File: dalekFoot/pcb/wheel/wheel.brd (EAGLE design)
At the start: 100 x 100 mm, 80 parts, among them IC1 LM1117MP-3.3, IC3 LM1117MP-3.3, IC4 4051D, IC5 4051D, IC6 LM1117MP-3.3, U1 TB6612FNG(O,C,8,EL, U2 SS8050-SOT-23, U3 SS8050-SOT-23, U4 SS8050-SOT-23, U5 TB6612FNG(O,C,8,EL, U6 TB6612FNG(O,C,8,EL

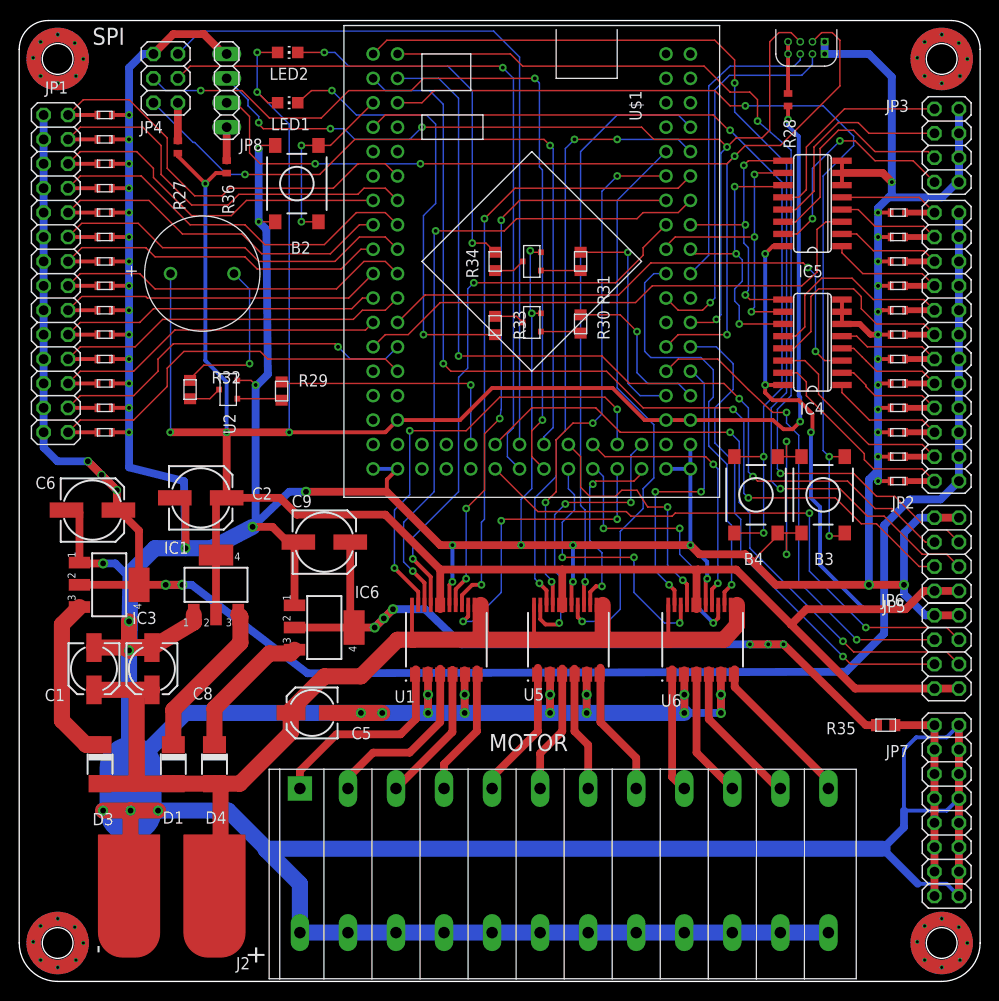
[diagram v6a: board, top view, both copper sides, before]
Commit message: optimize bottom route
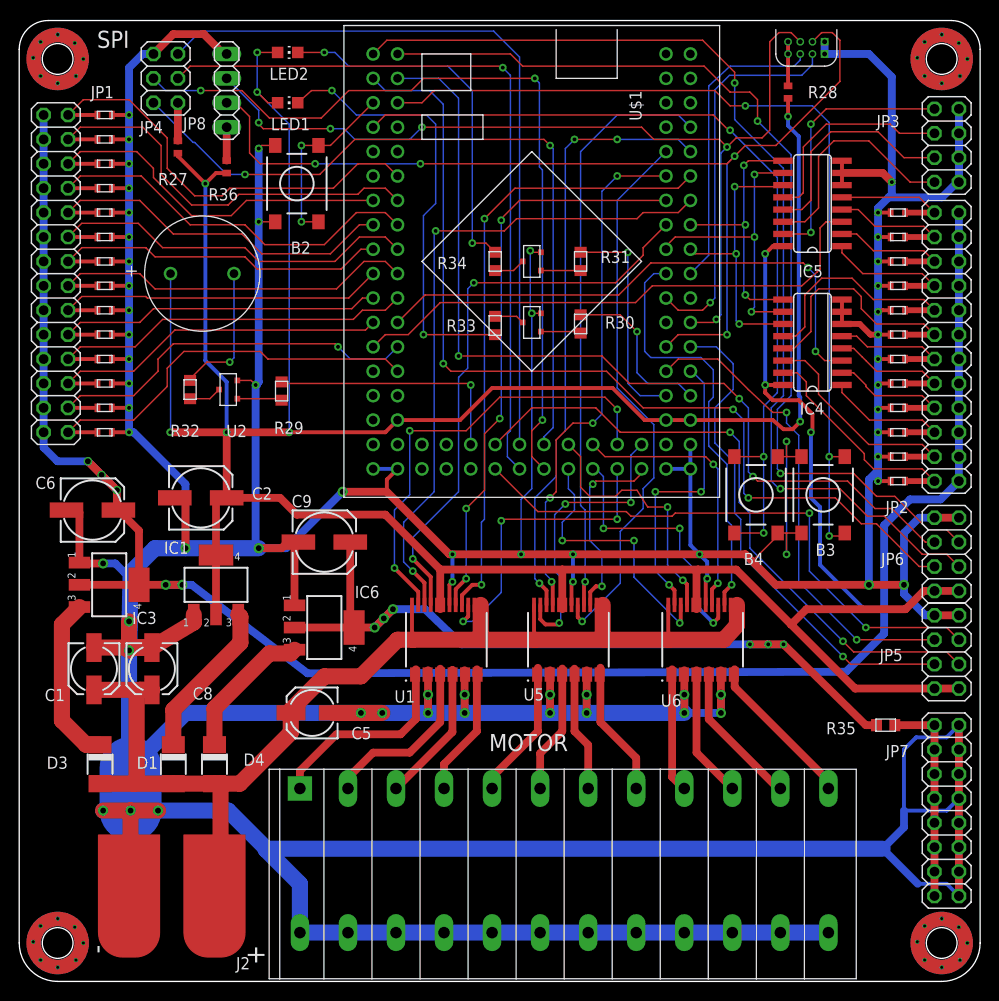
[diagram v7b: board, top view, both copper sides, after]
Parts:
- moved R28 0.79 mm to (80.0, 92.6)
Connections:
- net AIN0: now also IC5.15; no longer IC5.12
- net AIN1: now also IC5.12; no longer IC5.13
- net AIN2: now also IC5.13; no longer IC5.14
- net AIN3: now also IC5.14; no longer IC5.15
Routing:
- net AIN0: track 22.2 -> 27.8 mm, vias 0 -> 2
- net BUT2: track 96.5 -> 93.2 mm
- net N$18: track 17.0 -> 14.4 mm
- net DGND: track 866.5 -> 864.1 mm
- net BIN2.1: track 59.2 -> 57.6 mm
- net DIN1: track 109.0 -> 108.0 mm
- net AIN3.2: track 29.1 -> 28.2 mm
- net VCC-DIGITAL: track 340.0 -> 340.8 mm
- net N$7: track 5.38 -> 4.59 mm
- net MADC_A: track 29.7 -> 29.1 mm
- net AIN2: track 23.9 -> 23.2 mm
- net AIN1: track 22.7 -> 22.1 mm
- net AIN3: track 24.6 -> 24.2 mm, vias 2 -> 0

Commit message: optimize route and cover pour
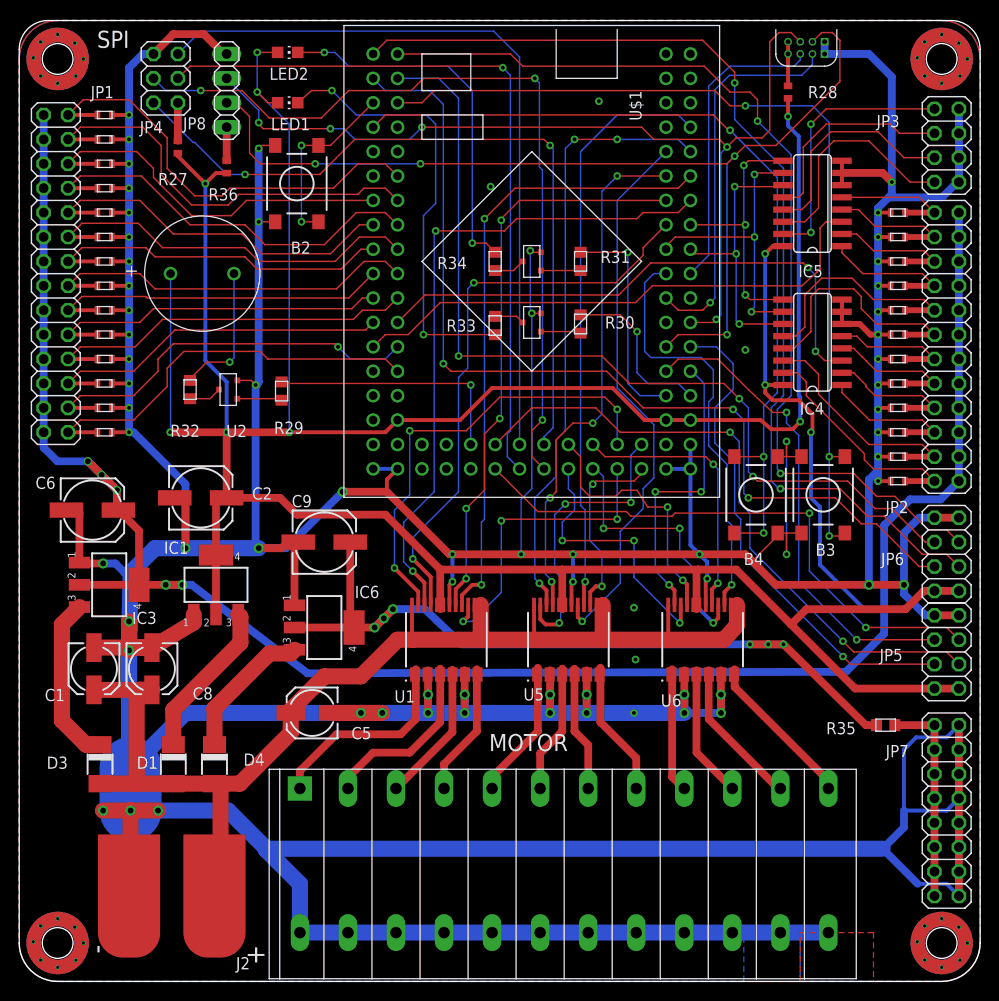
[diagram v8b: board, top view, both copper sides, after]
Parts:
- moved U$4 45.0 mm to (45.2, 36.8)
- moved U$3 33.2 mm to (61.6, 35.7)
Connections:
- net DGND: now also U$5.P$1, U$5.P$2, U$5.P$3, U$5.P$4, U$5.P$5, U$5.P$6, U$5.P$7, U$5.P$8, U$6.P$1, U$6.P$2, U$6.P$3, U$6.P$4, U$6.P$5, U$6.P$6, U$6.P$7, U$6.P$8, U$7.P$1, U$7.P$2, U$7.P$3, U$7.P$4, U$7.P$5, U$7.P$6, U$7.P$7, U$7.P$8, U$8.P$1, U$8.P$2, U$8.P$3, U$8.P$4, U$8.P$5, U$8.P$6, U$8.P$7, U$8.P$8
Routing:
- net DGND: vias 66 -> 72
- added copper zone on layer 1, net DGND
- added copper zone on layer 16, net DGND
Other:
- board text added: "VCC | SCK | NSS --------- MIS | MOS | GND"
- board text removed: "VCC | SCK | NSS -------------------- MIS | MOS | GND"
